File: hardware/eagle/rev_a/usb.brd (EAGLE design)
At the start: 47 x 21 mm, 0 parts

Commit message: finished usb schematic
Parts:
- added C1, C13, C14, C2, C3, C4, C5, C6: 22p, passives:0402_CAP
- added C10, C11, C9: 100u, passives:0402_CAP
- added C12: 0.1u, passives:0402_CAP
- added C7, C8: 27p, passives:0402_CAP
- added IC1: TUSB2036VF, BMO:VF_S-PQFP-G32
- added J1: MICRO_USB_B_HIROSE_ZX62-B-5PA(11), connector:USB_MICRO_B-HIROSE-ZX62-B-5PA(11)
- added P1, P2: 1932638-3_TE_AMP, BMO:1932638-3_TE_AMP
- added P3: USB-A-FEMALETESTPOINT, BMO:USB-A-TESTPOINT
- added R1, R13, R14, R2, R3, R4, R5, R6: 27, passives:0402_RES
- added R10, R11, R12, R7, R8, R9: 15k, passives:0402_RES
- added R15: 1.5k, passives:0402_RES
- added U1: TPS2043B, BMO:SO16
- added U2, U3, U4: SN75240, BMO:TSSOP8
- added X1: ABMM-6.000MHZ-B2-T, BMO:ABMM-6.000MHZ-B2-T
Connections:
- new net DM0: C14.1, IC1.2, R14.2, U4.4
- new net DP0: C13.1, IC1.1, R13.2, R15.1, U4.2
- new net DP0PUR: IC1.27, R15.2
- new net GND: C1.2, C10.2, C11.2, C12.2, C13.2, C14.2, C2.2, C3.2, C4.2, C5.2, C6.2, C7.2, C8.2, C9.2, IC1.21, IC1.22, IC1.23, IC1.24, IC1.28, IC1.31, IC1.7, J1.5, P1.4, P1.GND0, P1.GND1, P1.GND2, P1.GND3, P2.4, P2.GND0, P2.GND1, P2.GND2, P2.GND3, P3.GND, R10.1, R11.1, R12.1, R7.1, R8.1, R9.1, U1.1, U1.5, U2.1, U2.3, U2.5, U2.7, U3.1, U3.3, U3.5, U3.7, U4.1, U4.3, U4.5, U4.7, X1.2, X1.4
- new net N$1: C7.1, IC1.30, X1.1
- new net N$10: P2.2, R3.2
- new net N$11: P3.D+, R2.2, U2.6
- new net N$12: P3.D-, R1.2, U2.8
- new net N$13: IC1.9, U1.3
- new net N$14: IC1.13, U1.4
- new net N$15: IC1.17, U1.7
- new net N$16: C1.1, IC1.11, R1.1, R7.2
- new net N$17: IC1.10, U1.16
- new net N$18: C2.1, IC1.12, R2.1, R8.2
- new net N$19: IC1.14, U1.13
- new net N$2: C8.1, IC1.29, X1.3
- new net N$20: C5.1, IC1.19, R5.1, R9.2
- new net N$21: IC1.18, U1.12
- new net N$22: C6.1, IC1.20, R10.2, R6.1
- new net N$24: C4.1, IC1.15, R11.2, R3.1, U2.2
- new net N$25: C3.1, IC1.16, R12.2, R4.1, U2.4
- new net N$26: J1.2, R14.1
- new net N$27: J1.3, R13.1
- new net N$3: C11.1, P1.1, U1.11
- new net N$4: C10.1, P2.1, U1.14
- new net N$5: C9.1, P3.VCC, U1.15
- new net N$7: P1.2, R5.2, U3.2, U3.8
- new net N$8: P1.3, R6.2, U3.4, U3.6
- new net N$9: P2.3, R4.2
- new net VCC3V3: IC1.25, IC1.26, IC1.3, IC1.4, IC1.6, IC1.8
- new net VCC5V: C12.1, U1.2, U1.6
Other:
- outline, holes or cut-outs redrawn

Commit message: start of board, might need to restart
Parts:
- moved R15 231.8 mm to (18.0, 7.50), turned to 180 degrees
- moved U4 230.3 mm to (19.0, 12.0), turned to 90 degrees
- moved R14 220.1 mm to (21.5, 7.00), turned to 180 degrees
- moved R13 215.1 mm to (18.0, 6.50)
- moved C14 211.3 mm to (21.5, 6.00)
- moved C13 206.2 mm to (18.0, 5.50), turned to 180 degrees
- moved J1 205.5 mm to (-7.00, 13.5), flipped to the bottom, turned to 90 degrees
- moved C12 199.8 mm to (34.5, 11.5), flipped to the bottom, turned to 90 degrees
- moved X1 185.2 mm to (19.5, 5.00), flipped to the bottom
- moved C11 179.7 mm to (32.0, 3.50), turned to 270 degrees
- moved C10 176.7 mm to (35.5, 3.50), flipped to the bottom
- moved C9 174.3 mm to (35.5, 5.00), flipped to the bottom, turned to 90 degrees
- moved U3 170.8 mm to (41.0, 6.00), turned to 90 degrees
- moved R10 159.2 mm to (38.0, 15.5), flipped to the bottom
- moved U2 154.7 mm to (-2.00, 4.50), flipped to the bottom
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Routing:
- net N$27: track 0.00 -> 27.2 mm, vias 0 -> 3
- net N$25: track 0.00 -> 25.6 mm, vias 0 -> 2
- net VCC3V3: track 0.00 -> 24.9 mm, vias 0 -> 2
- net N$12: track 0.00 -> 21.2 mm, vias 0 -> 1
- net N$14: track 0.00 -> 20.5 mm, vias 0 -> 2
- net N$26: track 0.00 -> 19.5 mm, vias 0 -> 1
- net N$16: track 0.00 -> 19.5 mm, vias 0 -> 1
- net N$24: track 0.00 -> 17.4 mm, vias 0 -> 2
- net N$11: track 0.00 -> 17.3 mm, vias 0 -> 1
- net DM0: track 0.00 -> 15.9 mm, vias 0 -> 1
- net N$10: track 0.00 -> 13.7 mm
- net N$13: track 0.00 -> 13.6 mm, vias 0 -> 1
- net DP0PUR: track 0.00 -> 13.1 mm, vias 0 -> 1
- net N$1: track 0.00 -> 12.9 mm
- net N$4: track 0.00 -> 12.2 mm
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- added copper zone on layer 1, net GND
- added copper zone on layer 16, net GND
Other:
- board size 47 x 21 mm -> 51 x 22 mm

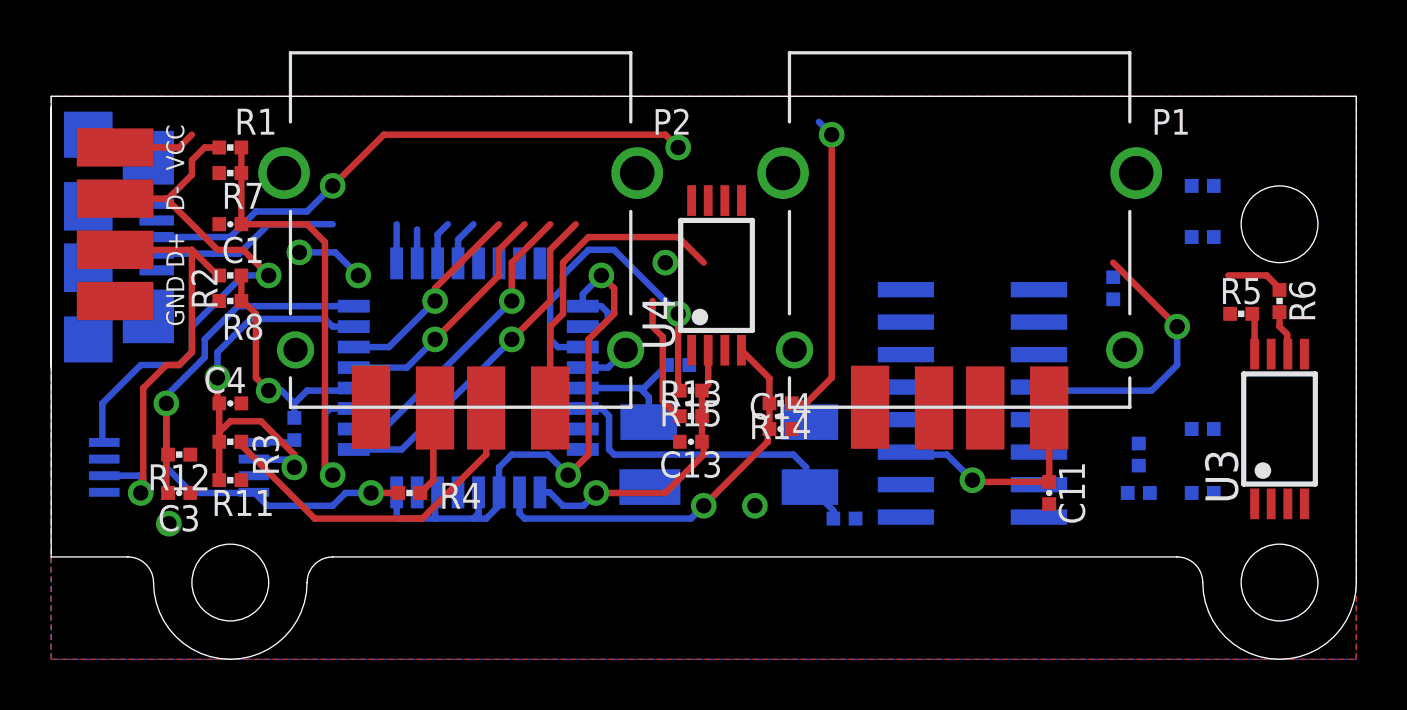
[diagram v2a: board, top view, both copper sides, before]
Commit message: usb board done
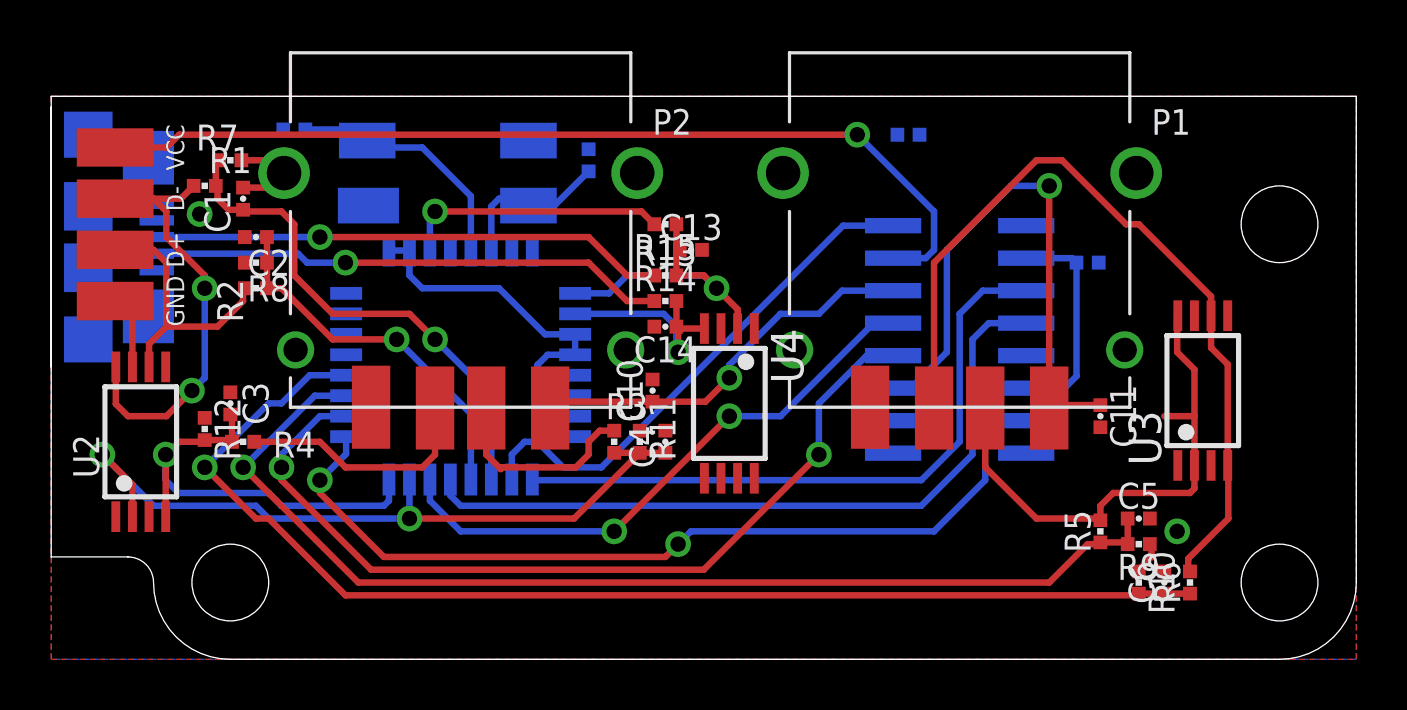
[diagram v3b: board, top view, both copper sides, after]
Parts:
- moved C10 19.4 mm to (16.5, 7.50), flipped to the top, turned to 90 degrees
- moved C8 17.6 mm to (2.50, 17.7), turned to 0 degrees
- moved C7 17.2 mm to (14.0, 16.5), turned to 90 degrees
- moved C4 17.1 mm to (17.0, 5.50), turned to 90 degrees
- moved R11 16.1 mm to (16.0, 5.50), turned to 270 degrees
- moved R10 15.7 mm to (35.5, 0.00), flipped to the top, turned to 270 degrees
- moved X1 15.6 mm to (8.50, 16.0)
- moved C9 15.4 mm to (26.5, 17.5), turned to 180 degrees
- moved R3 15.0 mm to (15.0, 5.50), turned to 90 degrees
- moved C6 13.6 mm to (36.5, 0.00), flipped to the top, turned to 90 degrees
- moved R6 11.5 mm to (37.5, 0.00), turned to 90 degrees
- moved R5 10.1 mm to (34.0, 2.00), turned to 90 degrees
- moved C2 7.65 mm to (1.00, 13.5), flipped to the top, turned to 180 degrees
- moved C13 7.50 mm to (18.0, 13.0), turned to 0 degrees
- moved R4 6.80 mm to (0.50, 5.50)
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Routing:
- net N$22: track 4.05 -> 47.6 mm, vias 0 -> 1
- net N$20: track 1.69 -> 43.3 mm, vias 0 -> 1
- net N$5: track 3.21 -> 36.7 mm, vias 0 -> 1
- net N$15: track 1.53 -> 34.6 mm, vias 0 -> 2
- net N$21: track 1.33 -> 34.1 mm, vias 0 -> 2
- net N$8: track 1.78 -> 32.1 mm
- net N$7: track 1.61 -> 20.4 mm
- net N$19: track 7.96 -> 22.8 mm, vias 1 -> 2
- net N$3: track 9.06 -> 22.5 mm
- net N$24: track 17.4 -> 29.5 mm
- net N$13: track 13.6 -> 25.3 mm, vias 1 -> 0
- net VCC5V: track 0.00 -> 8.71 mm
- net N$17: track 11.9 -> 20.4 mm, vias 1 -> 0
- net N$14: track 20.5 -> 28.9 mm, vias 2 -> 0
- net N$25: track 25.6 -> 17.5 mm, vias 2 -> 1
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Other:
- outline, holes or cut-outs redrawn

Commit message: tweaking size, added power header
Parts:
- added C15: 0.1u, passives:0402_CAP
- added JP1: (no value), SparkFun-Connectors:1X03
- moved C9 27.0 mm to (-0.50, 16.5), flipped to the top, turned to 0 degrees
- moved C2 4.00 mm to (0.80, 9.50), turned to 0 degrees
- moved R2 3.40 mm to (1.00, 8.10)
- moved R3 2.82 mm to (12.5, 4.20), turned to 180 degrees
- moved R7 2.24 mm to (1.00, 14.5)
- moved R8 2.20 mm to (1.00, 10.3), turned to 180 degrees
- moved J1 2.00 mm to (-5.00, 13.5)
- moved C1 1.58 mm to (1.00, 13.5), turned to 0 degrees
- moved C3 1.58 mm to (1.50, 6.50), turned to 0 degrees
- moved C4 1.58 mm to (15.5, 5.00)
- moved R11 1.58 mm to (14.5, 5.00)
- moved P3 1.50 mm to (-3.00, 17.0)
- moved R4 1.50 mm to (2.00, 5.50)
- moved R15 1.12 mm to (18.0, 14.5)
- moved R12 1.00 mm to (0.00, 6.00)
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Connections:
- net GND: now also C15.2, JP1.1
- net VCC3V3: now also C15.1, JP1.3
- net VCC5V: now also JP1.2
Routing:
- net VCC3V3: track 17.1 -> 59.9 mm
- net VCC5V: track 8.71 -> 17.8 mm
- net N$10: track 8.44 -> 4.69 mm
- net N$12: track 16.9 -> 20.7 mm
- net DP0: track 11.8 -> 14.4 mm
- net N$18: track 14.6 -> 16.7 mm
- net N$27: track 20.1 -> 18.1 mm
- net N$26: track 20.2 -> 18.2 mm
- net N$24: track 29.5 -> 27.6 mm
- net N$9: track 10.0 -> 8.51 mm
- net N$16: track 19.9 -> 18.8 mm
- net N$4: track 15.6 -> 16.7 mm
- net N$5: track 36.7 -> 37.7 mm
- net N$25: track 17.5 -> 16.5 mm
- net N$22: track 47.6 -> 48.6 mm
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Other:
- board size 51 x 22 mm -> 49 x 22 mm

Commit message: cleanup
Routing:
- net N$8: track 32.4 -> 33.6 mm
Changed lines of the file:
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@@
 <contactref element="JP1" pad="1"/>
 <via x="11.1" y="9.1" extent="1-16" drill="0.6"/>
+<wire x1="-2.675" y1="2.575" x2="-3.975" y2="2.575" width="0" layer="19" extent="1-1"/>
 </signal>
 <signal name="N$7">
@@
 <contactref element="U3" pad="2"/>
 <contactref element="P1" pad="2"/>
-<wire x1="37.675" y1="4.575" x2="37.675" y2="6.5" width="0.254" layer="1"/>
-<wire x1="37.675" y1="6.5" x2="37.675" y2="8.325" width="0.254" layer="1"/>
-<wire x1="37.675" y1="8.325" x2="37" y2="9" width="0.254" layer="1"/>
 <wire x1="37" y1="9" x2="37" y2="10.4" width="0.254" layer="1"/>
 <wire x1="37" y1="10.4" x2="37.025" y2="10.425" width="0.254" layer="1"/>
@@
 <wire x1="33.5" y1="2.93306875" x2="33.5" y2="4" width="0.254" layer="1"/>
 <wire x1="33.5" y1="4" x2="36" y2="6.5" width="0.254" layer="1"/>
-<wire x1="36" y1="6.5" x2="37.675" y2="6.5" width="0.254" layer="1"/>
+<wire x1="37.675" y1="4.575" x2="37.675" y2="5.325" width="0.254" layer="1"/>
+<wire x1="37.675" y1="5.325" x2="36" y2="7" width="0.254" layer="1"/>
+<wire x1="36" y1="7" x2="36" y2="8" width="0.254" layer="1"/>
+<wire x1="36" y1="8" x2="37" y2="9" width="0.254" layer="1"/>
+<wire x1="36" y1="6.5" x2="36" y2="7" width="0.254" layer="1"/>
 </signal>
 <signal name="N$8">
@@
 <contactref element="U3" pad="4"/>
 <contactref element="P1" pad="3"/>
-<wire x1="38.975" y1="4.575" x2="38.975" y2="8.525" width="0.254" layer="1"/>
-<wire x1="38.975" y1="8.525" x2="38.325" y2="9.175" width="0.254" layer="1"/>
+<wire x1="39" y1="8.5" x2="38.325" y2="9.175" width="0.254" layer="1"/>
 <wire x1="38.325" y1="10.425" x2="38.325" y2="9.175" width="0.254" layer="1"/>
 <wire x1="27.5" y1="6.82" x2="27.5" y2="12.5" width="0.254" layer="1"/>
@@
 <wire x1="36.5" y1="14" x2="38.325" y2="12.175" width="0.254" layer="1"/>
 <wire x1="38.325" y1="12.175" x2="38.325" y2="10.425" width="0.254" layer="1"/>
+<wire x1="38.975" y1="4.575" x2="38.975" y2="5.475" width="0.254" layer="1"/>
+<wire x1="38.975" y1="5.475" x2="40" y2="6.5" width="0.254" layer="1"/>
+<wire x1="40" y1="6.5" x2="40" y2="8" width="0.254" layer="1"/>
+<wire x1="40" y1="8" x2="39.5" y2="8.5" width="0.254" layer="1"/>
+<wire x1="39.5" y1="8.5" x2="39" y2="8.5" width="0.254" layer="1"/>
 </signal>
 <signal name="N$9">

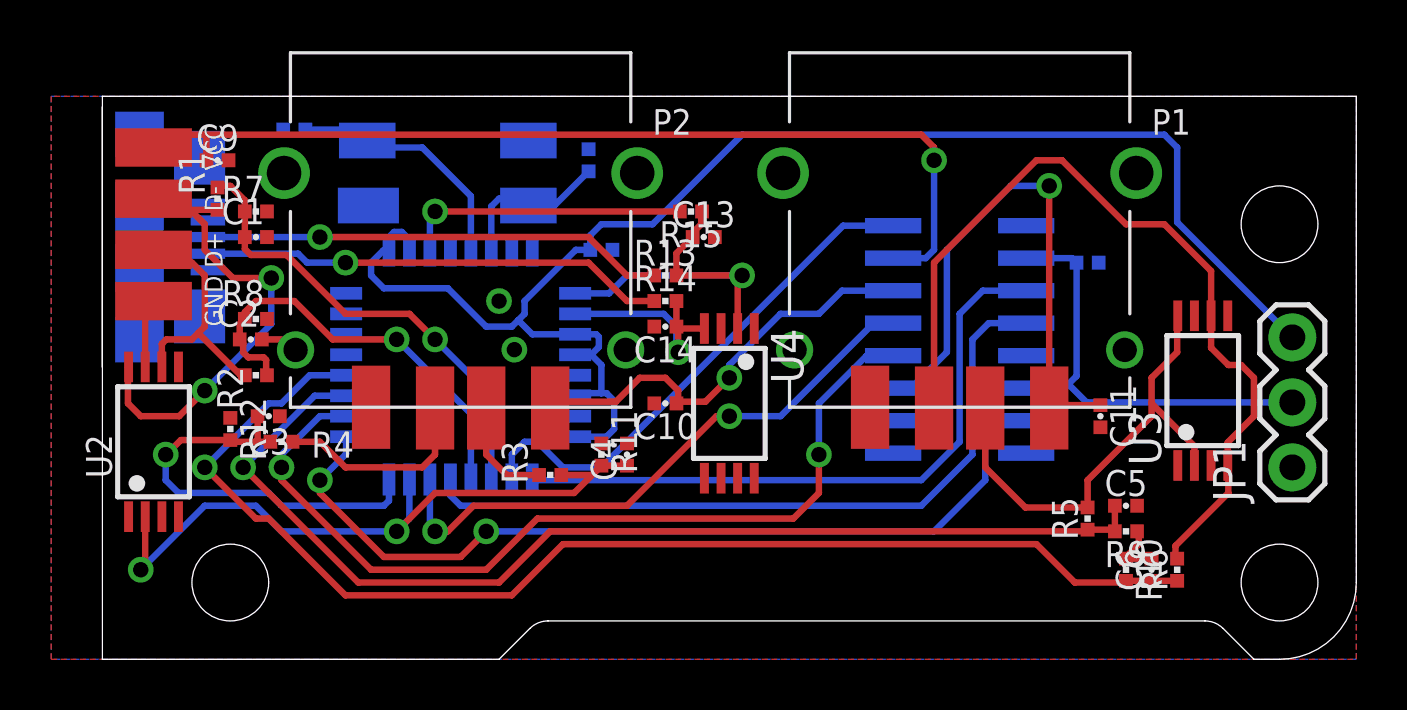
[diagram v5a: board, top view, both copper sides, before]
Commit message: Fitted board to case, added silkscreen
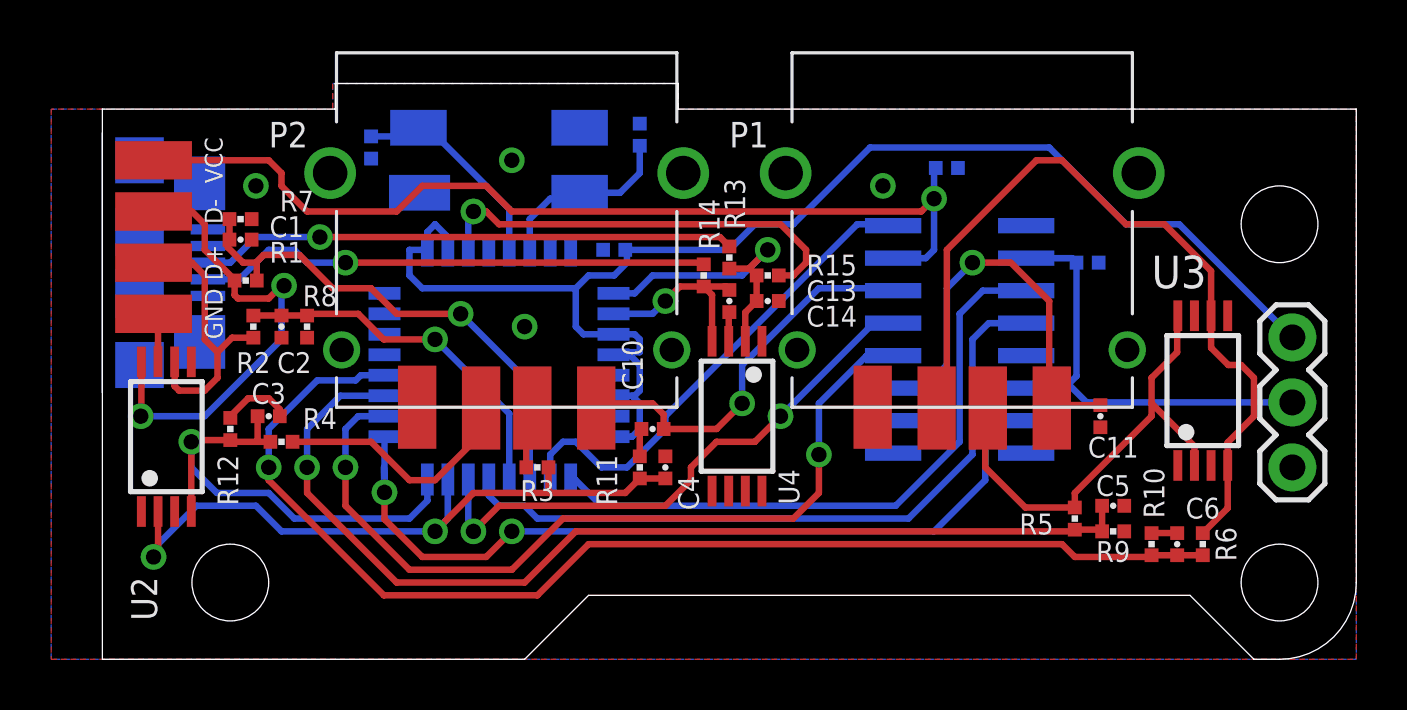
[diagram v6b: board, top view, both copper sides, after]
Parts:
- removed IC1: TUSB2036VF, BMO:VF_S-PQFP-G32
- added U5: TUSB2036VF, BMO:VF_S-PQFP-G32
- moved C9 28.5 mm to (28.0, 16.2), flipped to the bottom, turned to 180 degrees
- moved R15 3.91 mm to (21.0, 12.0), turned to 0 degrees
- moved C13 3.54 mm to (21.0, 11.0)
- moved R1 3.38 mm to (0.60, 11.8), turned to 180 degrees
- moved C8 3.08 mm to (5.50, 17.0), turned to 270 degrees
- moved C14 2.69 mm to (19.5, 11.0), turned to 270 degrees
- moved R13 2.60 mm to (19.5, 12.7), turned to 270 degrees
- moved C7 2.24 mm to (16.0, 17.5)
- moved X1 2.06 mm to (10.5, 16.5)
- moved R8 2.02 mm to (3.00, 10.0), turned to 90 degrees
- moved R2 1.90 mm to (0.90, 10.0), turned to 270 degrees
- moved R14 1.80 mm to (18.5, 12.0), turned to 270 degrees
- moved P2 1.80 mm to (10.8, 16.0)
- moved C4 1.58 mm to (17.0, 4.50)
- moved R11 1.58 mm to (16.0, 4.50)
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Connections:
- net DM0: now also U5.2; no longer IC1.2
- net DP0: now also U5.1; no longer IC1.1
- net DP0PUR: now also U5.27; no longer IC1.27
- net GND: now also U5.21, U5.22, U5.23, U5.24, U5.28, U5.31, U5.7; no longer IC1.21, IC1.22, IC1.23, IC1.24, IC1.28, IC1.31, IC1.7
- net N$1: now also U5.30; no longer IC1.30
- net N$13: now also U5.9; no longer IC1.9
- net N$14: now also U5.13; no longer IC1.13
- net N$15: now also U5.17; no longer IC1.17
- net N$16: now also U5.11; no longer IC1.11
- net N$17: now also U5.10; no longer IC1.10
- net N$18: now also U5.12; no longer IC1.12
- net N$19: now also U5.14; no longer IC1.14
- net N$2: now also U5.29; no longer IC1.29
- net N$20: now also U5.19; no longer IC1.19
- net N$21: now also U5.18; no longer IC1.18
- net N$22: now also U5.20; no longer IC1.20
- net N$24: now also U5.15; no longer IC1.15
- net N$25: now also U5.16; no longer IC1.16
- net VCC3V3: now also U5.25, U5.26, U5.3, U5.4, U5.6, U5.8; no longer IC1.25, IC1.26, IC1.3, IC1.4, IC1.6, IC1.8
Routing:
- net DP0PUR: track 11.2 -> 17.0 mm
- net N$3: track 22.5 -> 16.9 mm
- net VCC3V3: track 59.9 -> 56.2 mm
- net N$27: track 18.1 -> 20.9 mm
- net DP0: track 14.4 -> 11.7 mm
- net N$25: track 16.5 -> 19.1 mm
- net N$20: track 43.0 -> 40.5 mm
- net N$18: track 16.7 -> 14.2 mm
- net N$21: track 35.0 -> 32.7 mm
- net N$26: track 18.2 -> 20.1 mm
- net N$10: track 4.69 -> 2.84 mm
- net N$22: track 48.6 -> 46.8 mm
- net N$2: track 10.0 -> 8.48 mm
- net N$8: track 33.6 -> 32.2 mm
- net N$15: track 34.6 -> 33.3 mm
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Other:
- board size 49 x 22 mm -> 49 x 22.5 mm
- board text added: "BMO USB REV A Neal Jackson"
